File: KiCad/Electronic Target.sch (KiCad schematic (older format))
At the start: 44 parts, among them J1 BERG 2x6, J2 Conn_02x04_Odd_Even, U1 LM339, U2 74HC74, U3 74HC74, U4 74HC00, U5 74LV8154, U6 74LV8154, X1 8M0

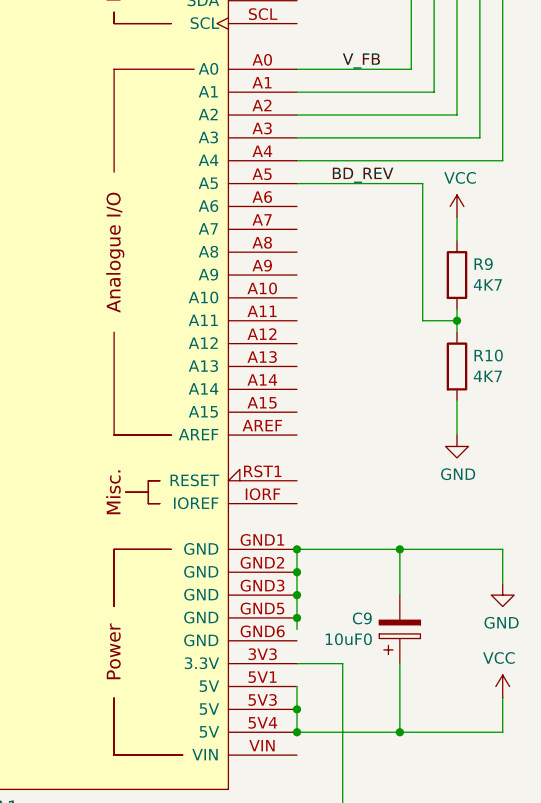
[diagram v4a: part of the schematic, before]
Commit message: Sensor Module
This commit updates the sensor module  for experimental evaluation
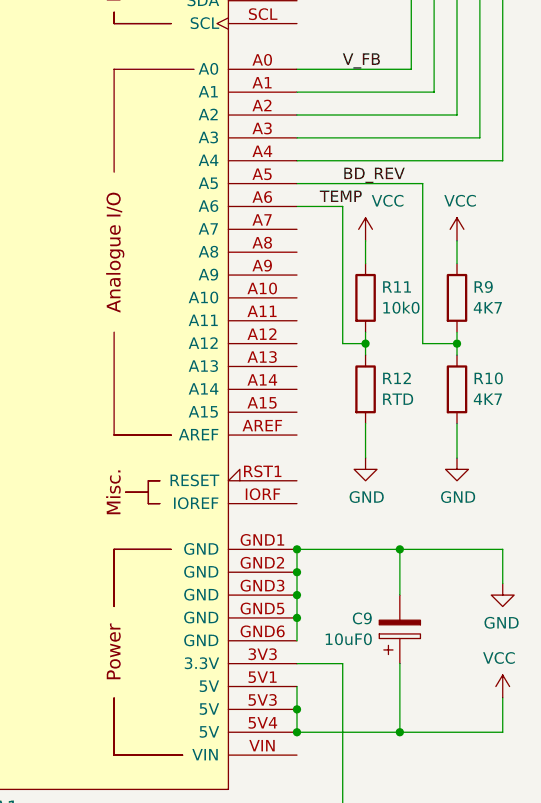
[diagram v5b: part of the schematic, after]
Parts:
- added R11: 10k0, Resistor_SMD:R_0805_2012Metric, symbol Device:R
- added R12: RTD, Connector_PinHeader_2.54mm:PinHeader_2x01_P2.54mm_Vertical, symbol Device:R
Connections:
- net GND: now also XA1.GND6 (GND), R12.2
- net VCC: now also R11.1
- net TEMP: now reaches XA1.A6
- net TEMP: now also R11.2, R12.1
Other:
- moved on the sheet: R10, R9
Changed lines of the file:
@@
 	15350 7200 15350 7100
 Connection ~ 15350 7100
-Wire Wire Line
-	15350 7250 15350 7200
 Connection ~ 15350 7200
 Wire Wire Line
@@
 L Device:R R9
 U 1 1 5F39A5E4
-P 16050 5700
-F 0 "R9" H 16120 5746 50  0000 L CNN
-F 1 "4K7" H 16120 5655 50  0000 L CNN
-F 2 "Resistor_SMD:R_0805_2012Metric" V 15980 5700 50  0001 C CNN
-F 3 "~" H 16050 5700 50  0001 C CNN
-	1    16050 5700
+P 16050 5800
+F 0 "R9" H 16120 5846 50  0000 L CNN
+F 1 "4K7" H 16120 5755 50  0000 L CNN
+F 2 "Resistor_SMD:R_0805_2012Metric" V 15980 5800 50  0001 C CNN
+F 3 "~" H 16050 5800 50  0001 C CNN
+	1    16050 5800
 	1    0    0    -1
 $EndComp
@@
 L Device:R R10
 U 1 1 5F39B55C
-P 16050 6100
-F 0 "R10" H 16120 6146 50  0000 L CNN
-F 1 "4K7" H 16120 6055 50  0000 L CNN
-F 2 "Resistor_SMD:R_0805_2012Metric" V 15980 6100 50  0001 C CNN
-F 3 "~" H 16050 6100 50  0001 C CNN
-	1    16050 6100
-	1    0    0    -1
-$EndComp
-Wire Wire Line
-	16050 5850 16050 5900
-Wire Wire Line
-	16050 5900 15900 5900
-Wire Wire Line
-	15900 5900 15900 5300
-Connection ~ 16050 5900
-Wire Wire Line
-	16050 5900 16050 5950
+P 16050 6200
+F 0 "R10" H 16120 6246 50  0000 L CNN
+F 1 "4K7" H 16120 6155 50  0000 L CNN
+F 2 "Resistor_SMD:R_0805_2012Metric" V 15980 6200 50  0001 C CNN
+F 3 "~" H 16050 6200 50  0001 C CNN
+	1    16050 6200
+	1    0    0    -1
+$EndComp
+Wire Wire Line
+	16050 5950 16050 6000
+Wire Wire Line
+	16050 6000 15900 6000
+Connection ~ 16050 6000
+Wire Wire Line
+	16050 6000 16050 6050
 $Comp
 L power:VCC #PWR019
 U 1 1 5F3D2998
-P 16050 5450
-F 0 "#PWR019" H 16050 5300 50  0001 C CNN
-F 1 "VCC" H 16065 5623 50  0000 C CNN
-F 2 "" H 16050 5450 50  0001 C CNN
-F 3 "" H 16050 5450 50  0001 C CNN
-	1    16050 5450
+P 16050 5550
+F 0 "#PWR019" H 16050 5400 50  0001 C CNN
+F 1 "VCC" H 16065 5723 50  0000 C CNN
+F 2 "" H 16050 5550 50  0001 C CNN
+F 3 "" H 16050 5550 50  0001 C CNN
+	1    16050 5550
 	1    0    0    -1
 $EndComp
@@
 L power:GND #PWR020
 U 1 1 5F3D3FD9
-P 16050 6400
-F 0 "#PWR020" H 16050 6150 50  0001 C CNN
-F 1 "GND" H 16055 6227 50  0000 C CNN
-F 2 "" H 16050 6400 50  0001 C CNN
-F 3 "" H 16050 6400 50  0001 C CNN
-	1    16050 6400
-	1    0    0    -1
-$EndComp
-Wire Wire Line
-	16050 5450 16050 5550
-Wire Wire Line
-	16050 6250 16050 6400
-Wire Wire Line
-	15350 5300 15900 5300
-Text Label 15500 5300 0    50   ~ 0
+P 16050 6500
+F 0 "#PWR020" H 16050 6250 50  0001 C CNN
+F 1 "GND" H 16055 6327 50  0000 C CNN
+F 2 "" H 16050 6500 50  0001 C CNN
+F 3 "" H 16050 6500 50  0001 C CNN
+	1    16050 6500
+	1    0    0    -1
+$EndComp
+Wire Wire Line
+	16050 5550 16050 5650
+Wire Wire Line
+	16050 6350 16050 6500
+Text Label 15550 5300 0    50   ~ 0
 BD_REV
 Wire Wire Line
 	1200 1800 1200 8250
 Connection ~ 1200 1800
+$Comp
+L Device:R R11
+U 1 1 5E7B2625
+P 15650 5800
+F 0 "R11" H 15720 5846 50  0000 L CNN
+F 1 "10k0" H 15720 5755 50  0000 L CNN
+F 2 "Resistor_SMD:R_0805_2012Metric" V 15580 5800 50  0001 C CNN
+F 3 "~" H 15650 5800 50  0001 C CNN
+	1    15650 5800
+	1    0    0    -1
+$EndComp
+$Comp
+L Device:R R12
+U 1 1 5E7B3570
+P 15650 6200
+F 0 "R12" H 15720 6246 50  0000 L CNN
+F 1 "RTD" H 15720 6155 50  0000 L CNN
+F 2 "Connector_PinHeader_2.54mm:PinHeader_2x01_P2.54mm_Vertical" V 15580 6200 50  0001 C CNN
+F 3 "~" H 15650 6200 50  0001 C CNN
+	1    15650 6200
+	1    0    0    -1
+$EndComp
+Wire Wire Line
+	15650 6050 15650 6000
+Wire Wire Line
+	15650 6000 15550 6000
+Connection ~ 15650 6000
+Wire Wire Line
+	15650 6000 15650 5950
+$Comp
+L power:GND #PWR022
+U 1 1 5E8CAB18
+P 15650 6500
+F 0 "#PWR022" H 15650 6250 50  0001 C CNN
+F 1 "GND" H 15655 6327 50  0000 C CNN
+F 2 "" H 15650 6500 50  0001 C CNN
+F 3 "" H 15650 6500 50  0001 C CNN
+	1    15650 6500
+	1    0    0    -1
+$EndComp
+$Comp
+L power:VCC #PWR021
+U 1 1 5E8CBA58
+P 15650 5550
+F 0 "#PWR021" H 15650 5400 50  0001 C CNN
+F 1 "VCC" H 15748 5723 50  0000 C CNN
+F 2 "" H 15650 5550 50  0001 C CNN
+F 3 "" H 15650 5550 50  0001 C CNN
+	1    15650 5550
+	1    0    0    -1
+$EndComp
+Wire Wire Line
+	15900 5300 15350 5300
+Wire Wire Line
+	15900 5300 15900 6000
+Wire Wire Line
+	15550 5400 15350 5400
+Wire Wire Line
+	15550 5400 15550 6000
+Wire Wire Line
+	15650 5550 15650 5650
+Wire Wire Line
+	15650 6350 15650 6500
+Wire Wire Line
+	15350 7200 15350 7300
+Text Label 15450 5400 0    50   ~ 0
+TEMP
 $EndSCHEMATC

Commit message: Circuit Rev 2
Added negative power supply to drive sensor boards
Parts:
- removed J1: BERG 2x6, Connector_PinHeader_2.54mm:PinHeader_2x06_P2.54mm_Vertical, symbol Connector_Generic:Conn_2Rows-11Pins
- removed R11: 10k0, Resistor_SMD:R_0805_2012Metric, symbol Device:R
- removed R12: RTD, Connector_PinHeader_2.54mm:PinHeader_2x01_P2.54mm_Vertical, symbol Device:R
- added J1: Conn_02x06_Odd_Even, Connector_PinHeader_2.54mm:PinHeader_2x06_P2.54mm_Vertical, symbol Connector_Generic:Conn_02x06_Odd_Even
- added U7: NMA0505SC, NMA0505SC:SIP600W50P254L1950H1000Q5, symbol NMA0505SC:NMA0505SC
- R10, R9: footprint Resistor_SMD:R_0805_2012Metric -> (none)
- TP3: value SO -> TP
- TP4: value WE -> TP
- renumbered NO1 to TP1, GND1 to TP10, EA1 to TP2, RN1 to TP5, RE1 to TP6, RS1 to TP7, RW1 to TP8, VCC1 to TP9
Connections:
- net GND: now also J1.7 (Pin_7), J1.9 (Pin_9), U7.2 (-VIN), U7.5 (0V); no longer XA1.GND6 (GND)
- net MIC_EAST: now also J1.4 (Pin_4)
- net MIC_NORTH: now also J1.2 (Pin_2)
- net MIC_SOUTH: now also J1.6 (Pin_6)
- net MIC_WEST: now also J1.8 (Pin_8)
- net TEMP: now also J1.12 (Pin_12)
- net VCC: now also J1.1 (Pin_1), J1.3 (Pin_3), J1.5 (Pin_5), U7.1 (+VIN)
- net at XA1.3V3 (3.3V): no longer C10.1
- new net: C10.1, J1.10 (Pin_10), J1.11 (Pin_11), U7.4 (-VOUT)
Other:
- moved on the sheet: C2, C3, C4, C5, C6, C7, C8, R10, R9, TP10, TP9, U1E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

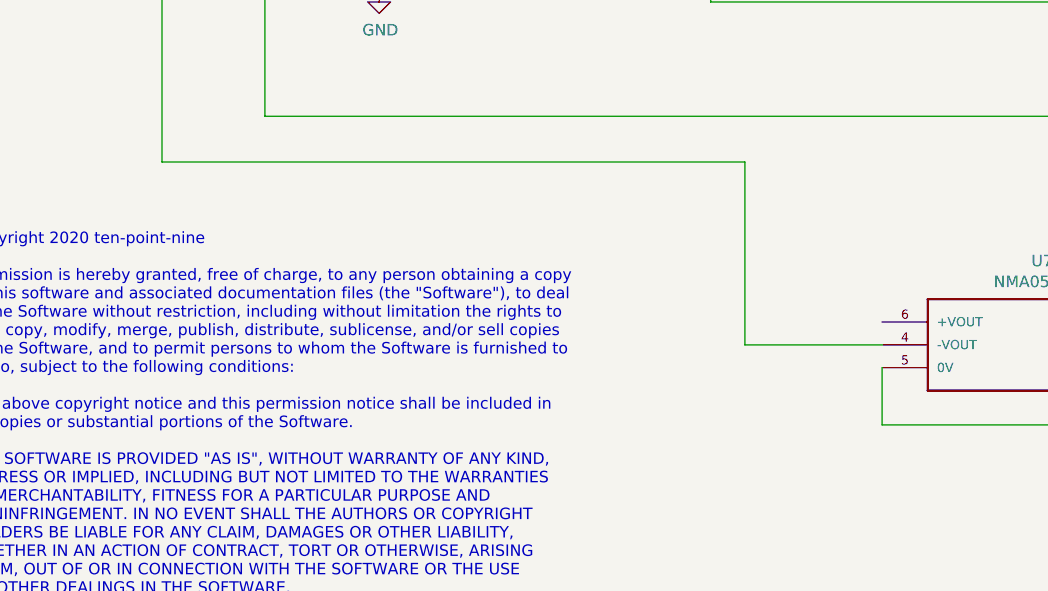
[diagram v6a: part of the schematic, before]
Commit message: Corrections to PCB
Added load resistor to switching power supply
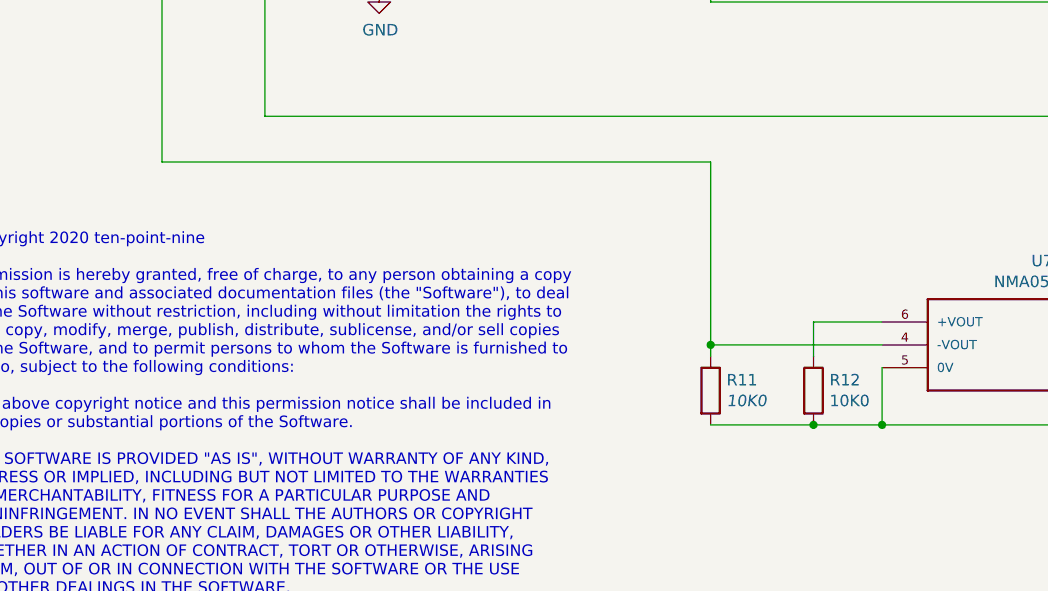
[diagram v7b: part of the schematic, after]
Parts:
- added R11, R12: 10K0, Resistor_SMD:R_0805_2012Metric, symbol Device:R
- R10, R9: footprint (none) -> Resistor_SMD:R_0805_2012Metric
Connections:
- net GND: now also R11.2, R12.2
- net at C10.1, J1.10 (Pin_10), J1.11 (Pin_11)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: now also R11.1
- net at U7.6 (+VOUT): now also R12.1
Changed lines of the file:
@@
 F 0 "R9" H 16120 5746 50  0000 L CNN
 F 1 "4K7" H 16120 5655 50  0000 L CNN
-F 2 "" V 15980 5700 50  0001 C CNN
+F 2 "Resistor_SMD:R_0805_2012Metric" V 15980 5700 50  0001 C CNN
 F 3 "~" H 16050 5700 50  0001 C CNN
 	1    16050 5700
@@
 F 0 "R10" H 16120 6146 50  0000 L CNN
 F 1 "4K7" H 16120 6055 50  0000 L CNN
-F 2 "" V 15980 6100 50  0001 C CNN
+F 2 "Resistor_SMD:R_0805_2012Metric" V 15980 6100 50  0001 C CNN
 F 3 "~" H 16050 6100 50  0001 C CNN
 	1    16050 6100
@@
 	1500 1800 1500 8400
 Wire Wire Line
-	1500 8400 4050 8400
+	3900 8400 3900 9200
+Connection ~ 1500 1800
+$Comp
+L Device:R R11
+U 1 1 5EAD205F
+P 3900 9400
+F 0 "R11" H 3970 9446 50  0000 L CNN
+F 1 "10K0" H 3970 9355 50  0000 L CIN
+F 2 "Resistor_SMD:R_0805_2012Metric" V 3830 9400 50  0001 C CNN
+F 3 "~" H 3900 9400 50  0001 C CNN
+	1    3900 9400
+	1    0    0    -1
+$EndComp
+$Comp
+L Device:R R12
+U 1 1 5EAD3F6F
+P 4350 9400
+F 0 "R12" H 4420 9446 50  0000 L CNN
+F 1 "10K0" H 4420 9355 50  0000 L CNN
+F 2 "Resistor_SMD:R_0805_2012Metric" V 4280 9400 50  0001 C CNN
+F 3 "~" H 4350 9400 50  0001 C CNN
+	1    4350 9400
+	1    0    0    -1
+$EndComp
 Wire Wire Line
-	4050 8400 4050 9200
+	4650 9100 4350 9100
 Wire Wire Line
-	4050 9200 4650 9200
-Connection ~ 1500 1800
+	4350 9100 4350 9250
+Wire Wire Line
+	3900 9200 3900 9250
+Connection ~ 3900 9200
+Connection ~ 4650 9550
+Wire Wire Line
+	4350 9550 4650 9550
+Wire Wire Line
+	1500 8400 3900 8400
+Wire Wire Line
+	3900 9200 4650 9200
+Wire Wire Line
+	3900 9550 4350 9550
+Connection ~ 4350 9550
 $EndSCHEMATC

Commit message: Using digital thermometer
Changes to the circuit to support an I2C termometer in place of the RTD
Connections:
- net GND: now also J1.5 (Pin_5); no longer J1.9 (Pin_9)
- net VCC: no longer J1.5 (Pin_5)
- net SCL: now reaches XA1.SCL
- net SCL: now also J1.12 (Pin_12)
- net SDA: now reaches XA1.SDA
- net SDA: now also J1.10 (Pin_10)
- net at C10.1, J1.11 (Pin_11), R11.1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: now also J1.9 (Pin_9); no longer J1.10 (Pin_10)
- net TEMP: no longer names the net of XA1.A6
- net TEMP: no longer J1.12 (Pin_12)
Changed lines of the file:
@@
 MIC_WEST
 Wire Wire Line
-	600  1400 700  1400
-Wire Wire Line
-	600  1400 600  1300
-Wire Wire Line
 	600  1300 700  1300
 Wire Wire Line
@@
 Wire Wire Line
 	600  1200 700  1200
-Connection ~ 600  1300
 $Comp
 L power:VCC #PWR01
@@
 Wire Wire Line
 	700  1500 600  1500
-Wire Wire Line
-	600  1500 600  1600
-Wire Wire Line
-	700  1600 600  1600
 $Comp
 L power:GND #PWR02
@@
 Wire Wire Line
 	850  2250 600  2250
-Wire Wire Line
-	600  2250 600  1600
 Connection ~ 600  2250
-Connection ~ 600  1600
 Connection ~ 850  1800
 Wire Wire Line
@@
 	1    0    0    -1
 $EndComp
-Wire Wire Line
-	1200 1600 1500 1600
-Wire Wire Line
-	1500 1600 1500 1800
 Wire Wire Line
 	10850 8700 11650 8700
@@
 	850  1800 1500 1800
 Wire Wire Line
-	1200 1700 1950 1700
-Wire Wire Line
-	16400 8200 16400 6700
-Wire Wire Line
-	16400 6700 15750 6700
-Wire Wire Line
-	15750 6700 15750 5400
-Wire Wire Line
-	15350 5400 15750 5400
-Text Label 15500 5400 0    50   ~ 0
-TEMP
-Wire Wire Line
-	1950 1700 1950 8200
-Wire Wire Line
-	1950 8200 16400 8200
-Wire Wire Line
 	1500 1800 1500 8400
 Wire Wire Line
 	3900 8400 3900 9200
-Connection ~ 1500 1800
 $Comp
 L Device:R R11
@@
 	3900 9550 4350 9550
 Connection ~ 4350 9550
+Wire Wire Line
+	600  1500 600  2250
+Wire Wire Line
+	700  1400 600  1400
+Wire Wire Line
+	600  1400 600  1500
+Connection ~ 600  1500
+Wire Wire Line
+	700  1600 700  1700
+Connection ~ 700  1700
+Wire Wire Line
+	15700 4500 15350 4500
+Wire Wire Line
+	15700 4600 15350 4600
+Text Label 15450 4500 0    50   ~ 0
+SDA
+Text Label 15450 4600 0    50   ~ 0
+SCL
+Wire Wire Line
+	1200 1700 1700 1700
+Wire Wire Line
+	1200 1600 1700 1600
+Text Label 1350 1600 0    50   ~ 0
+SDA
+Text Label 1350 1700 0    50   ~ 0
+SCL
 $EndSCHEMATC
